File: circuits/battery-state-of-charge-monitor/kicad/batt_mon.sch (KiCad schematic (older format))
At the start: 9 parts

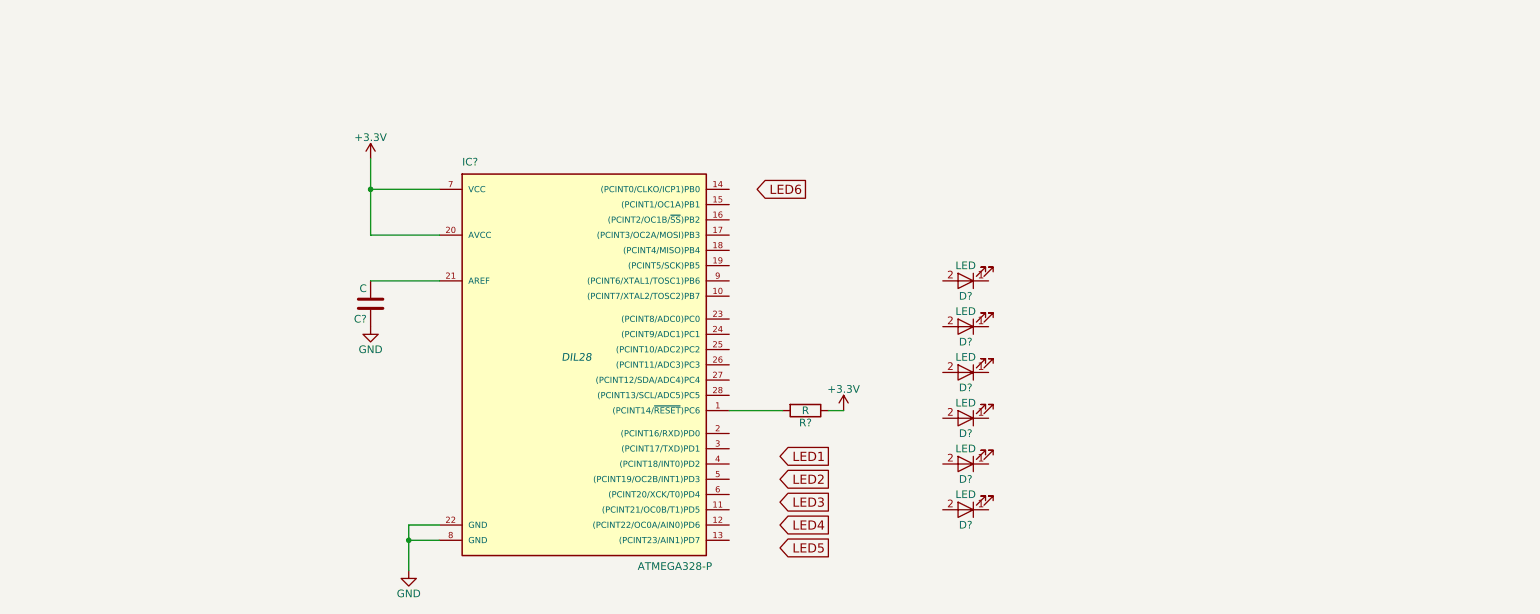
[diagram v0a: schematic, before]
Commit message: added 2950 voltage reg and switch to battery
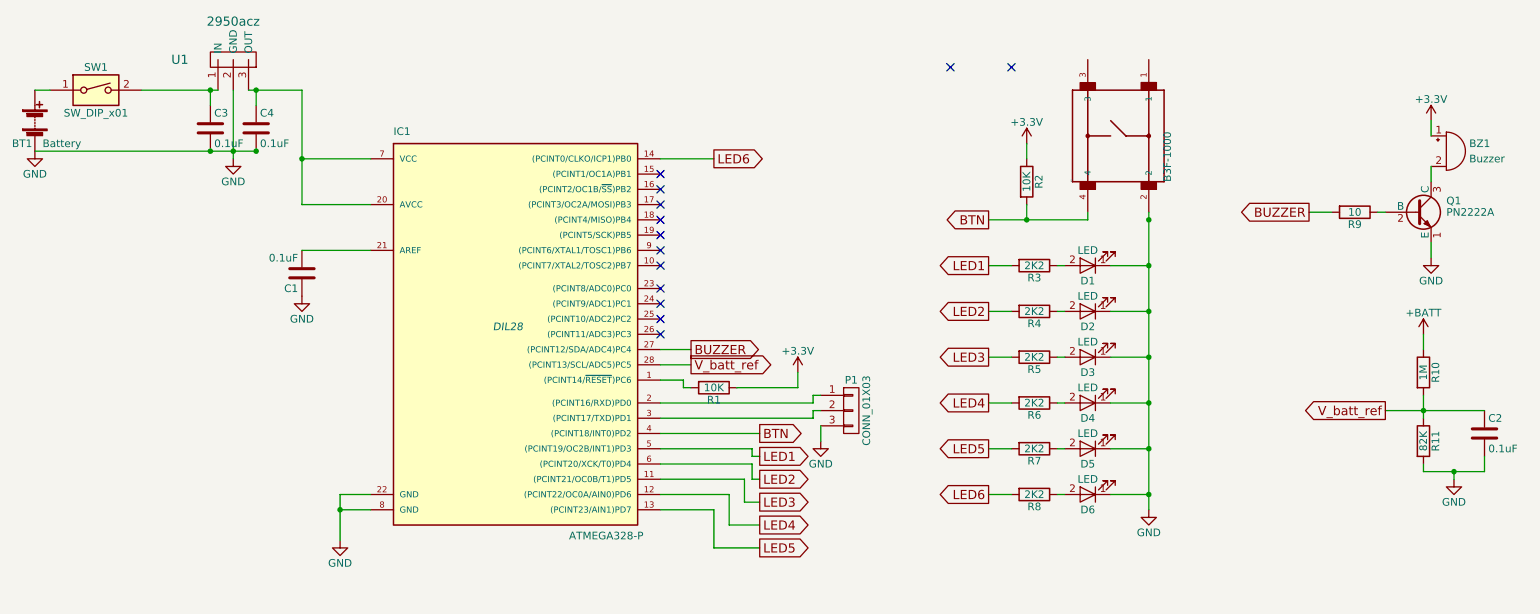
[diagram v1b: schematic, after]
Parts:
- added BT1: Battery, symbol Battery
- added BZ1: Buzzer, symbol Buzzer
- added C2, C3, C4: 0.1uF, symbol C
- added P1: CONN_01X03, symbol CONN_01X03
- added Q1: PN2222A, symbol PN2222A
- added R10: 1M, symbol R
- added R11: 82K, symbol R
- added R2: 10K, symbol R
- added R3, R4, R5, R6, R7, R8: 2K2, symbol R
- added R9: 10, symbol R
- added S1: B3F-1000, SW_B3F-1000, symbol B3F-1000
- added SW1: SW_DIP_x01, symbol SW_DIP_x01
- added U1: 2950acz, symbol 2950acz
- C1: renamed from C?; value C -> 0.1uF
- R1: renamed from R?; value R -> 10K
- gave numbers to parts that had none: 7
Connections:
- net +3V3: now also BZ1.1 (-), R2.1; no longer IC1.20 (AVCC), IC1.7 (VCC)
- net GND: now also D1.1 (K), D2.1 (K), D3.1 (K), D4.1 (K), D5.1 (K), D6.1 (K), BT1.2 (-), C2.2, C3.2, C4.2, P1.3 (P3), Q1.1 (E), R11.2, S1.2, U1.2 (GND)
- net LED1: now also IC1.5 ((PCINT19/OC2B/INT1)PD3), R3.2
- net LED2: now also IC1.6 ((PCINT20/XCK/T0)PD4), R4.2
- net LED3: now also IC1.11 ((PCINT21/OC0B/T1)PD5), R5.2
- net LED4: now also IC1.12 ((PCINT22/OC0A/AIN0)PD6), R6.2
- net LED5: now also IC1.13 ((PCINT23/AIN1)PD7), R7.2
- net LED6: now also IC1.14 ((PCINT0/CLKO/ICP1)PB0), R8.2
- net at IC1.2 ((PCINT16/RXD)PD0): now also P1.1 (P1)
- net BUZZER: now reaches IC1.27 ((PCINT12/SDA/ADC4)PC4)
- net BUZZER: now also R9.2
- net V_batt_ref: now reaches IC1.28 ((PCINT13/SCL/ADC5)PC5)
- net V_batt_ref: now also C2.1, R10.2, R11.1
- net at IC1.3 ((PCINT17/TXD)PD1): now also P1.2 (P2)
- net BTN: now reaches IC1.4 ((PCINT18/INT0)PD2)
- net BTN: now also R2.2, S1.4
- net at D1.2 (A): now also R3.1
- net at D2.2 (A): now also R4.1
- net at D3.2 (A): now also R5.1
- net at D4.2 (A): now also R6.1
- net at D5.2 (A): now also R7.1
- net at D6.2 (A): now also R8.1
- new net: C4.1, IC1.20 (AVCC), IC1.7 (VCC), U1.3 (OUT)
- new net: Q1.2 (B), R9.1
- new net: BZ1.2 (+), Q1.3 (C)
- new net: C3.1, SW1.2, U1.1 (IN)
- new net: BT1.1 (+), SW1.1
- new net +BATT: R10.1
- no-connect marks 0 -> 13
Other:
- moved on the sheet: C1, D1, D2, D3, D4, D5, D6, IC1, R1
